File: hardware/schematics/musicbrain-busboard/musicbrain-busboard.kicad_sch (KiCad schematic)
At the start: 96 parts, among them J1 SLOT 1, J10 EXP, J11 DISPLAY, J12 QWIIC, J13 MIDI IN1, J14 MIDI IN2, J15 MIDI OUT, J16 CAN, J17 AUDIO/CODEC, J18 TUNE, J19 DLG1 (Serial3), J2 SLOT 2, J20 DLG2 (Serial4), J21 EXPANSION, J22 MIDI OUT2, J23 USB HOST, J24 AUDIOHUB, J3 SLOT 3, J4 SLOT 4, J5 SLOT 5, J6 SLOT 6, J7 HUB 1, J8 HUB 2, J9 PWR IN, U1 Teensy 4.1, U10 H11L1, U11 74LVC1G17, U12 SN65HVD230, U13 74LVC1G17, U14 74LVC1G17, U2 R-78E5.0-1.0, U3 AMS1117-3.3, U4 74HC154, U5 74HC165, U6 74HC165, U7 74LVC1G125, U8 74LVC245, U9 H11L1

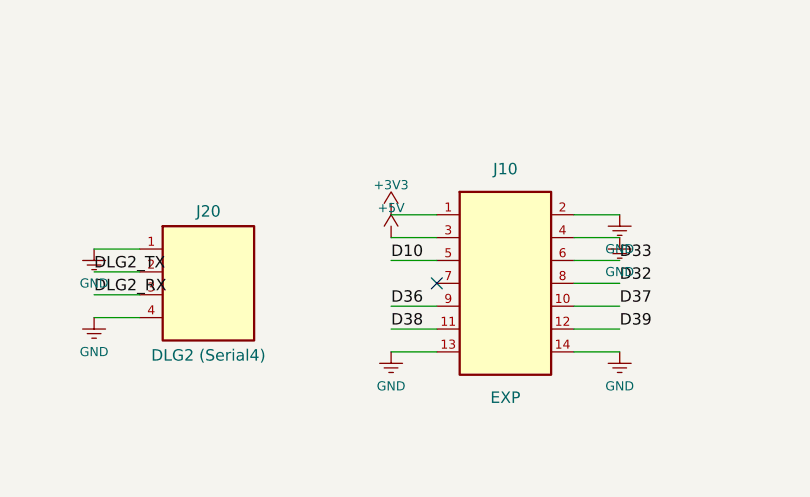
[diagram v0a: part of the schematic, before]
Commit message: busboard rev 3.1: J25 Axon-voedingsheader (+5V/GND naast J19)
Pin 1 landt op het +5V-spoor van de SES-bundel, pin 2 GND-stub naar de
GND-verticaal (x=70); geen herroute — ERC 0, netcheck OK, DRC 0/0.
Fab-pakket + assets + pinout J25 + README/MODULES bijgewerkt.

Co-Authored-By: Claude Fable 5 <noreply@anthropic.com>
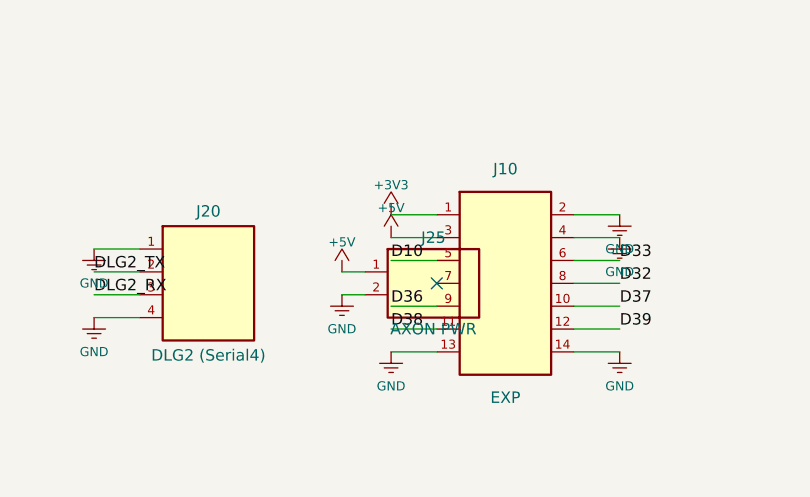
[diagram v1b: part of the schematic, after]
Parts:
- added J17: AUDIO/CODEC, Connector_PinHeader_2.54mm:PinHeader_2x07_P2.54mm_Vertical, symbol Custom:Conn_02x07
- J25: renamed from J17; value AUDIO/CODEC -> AXON PWR; footprint Connector_PinHeader_2.54mm:PinHeader_2x07_P2.54mm_Vertical -> Connector_PinHeader_2.54mm:PinHeader_1x02_P2.54mm_Vertical; symbol Custom:Conn_02x07 -> Custom:Conn_01x02
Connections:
- net +12V: now also J17.11 (Pin_11); no longer J25.11 (Pin_11)
- net +3V3: now also J17.1 (Pin_1); no longer J25.1 (Pin_1)
- net +5V: now also J25.1 (Pin_1), J17.3 (Pin_3); no longer J25.3 (Pin_3)
- net -12V: now also J17.13 (Pin_13); no longer J25.13 (Pin_13)
- net BCLK: now also J17.6 (Pin_6); no longer J25.6 (Pin_6)
- net CODEC_RST: now also J17.2 (Pin_2); no longer J25.2 (Pin_2)
- net GND: now also J25.2 (Pin_2), J17.14 (Pin_14), J17.5 (Pin_5), J17.7 (Pin_7), J17.9 (Pin_9); no longer J25.14 (Pin_14), J25.5 (Pin_5), J25.7 (Pin_7), J25.9 (Pin_9)
- net I2S_IN: now also J17.12 (Pin_12); no longer J25.12 (Pin_12)
- net I2S_OUT: now also J17.10 (Pin_10); no longer J25.10 (Pin_10)
- net LRCLK: now also J17.8 (Pin_8); no longer J25.8 (Pin_8)
- net MCLK: now also J17.4 (Pin_4); no longer J25.4 (Pin_4)
